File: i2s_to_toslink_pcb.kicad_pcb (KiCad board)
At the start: 2 copper layers, 61.7 x 62.7 mm, 74 parts, among them J1 FTDI_6P, J10 FCR684204T, J11 DIN_DOUT_2TP, J12 MCU_GPIOS, J13 AJ_TP5, J14 C_G0, J15 C_G7, J16 CRST, J17 C_CLKOUT, J2 EXT_CLK_IN5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

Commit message: routing cleanups
Signed-off-by: Mika Laitio <lamikr@gmail.com>
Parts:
- moved C20 3.11 mm to (41.5, 40.3), turned to -90 degrees
- moved R19 2.60 mm to (33.4, 56.0)
- moved R20 2.60 mm to (33.4, 53.4)
- moved J8 1.50 mm to (25.5, 39.0)
- moved C13 1.48 mm to (24.3, 43.3)
- moved U3 1.08 mm to (31.3, 46.7)
- moved C14 1.08 mm to (24.8, 48.9)
- moved C15 1.08 mm to (37.8, 47.6)
- moved C16 1.08 mm to (37.8, 45.0)
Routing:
- net VCC_3V3: track 230.4 -> 222.6 mm
- net Net-(J9-Pin_3): track 28.4 -> 25.7 mm
- net MCU_SDA1: track 56.8 -> 58.7 mm
- net GND: track 95.7 -> 97.6 mm, vias 30 -> 29
- net Net-(J3-Pin_2): track 23.4 -> 25.0 mm
- net EXTERNAL_IN_I2S_BCLK: track 62.1 -> 61.0 mm
- net Net-(J7-Pin_3): track 19.6 -> 18.5 mm
- net MCU_SCL1: track 48.5 -> 49.0 mm

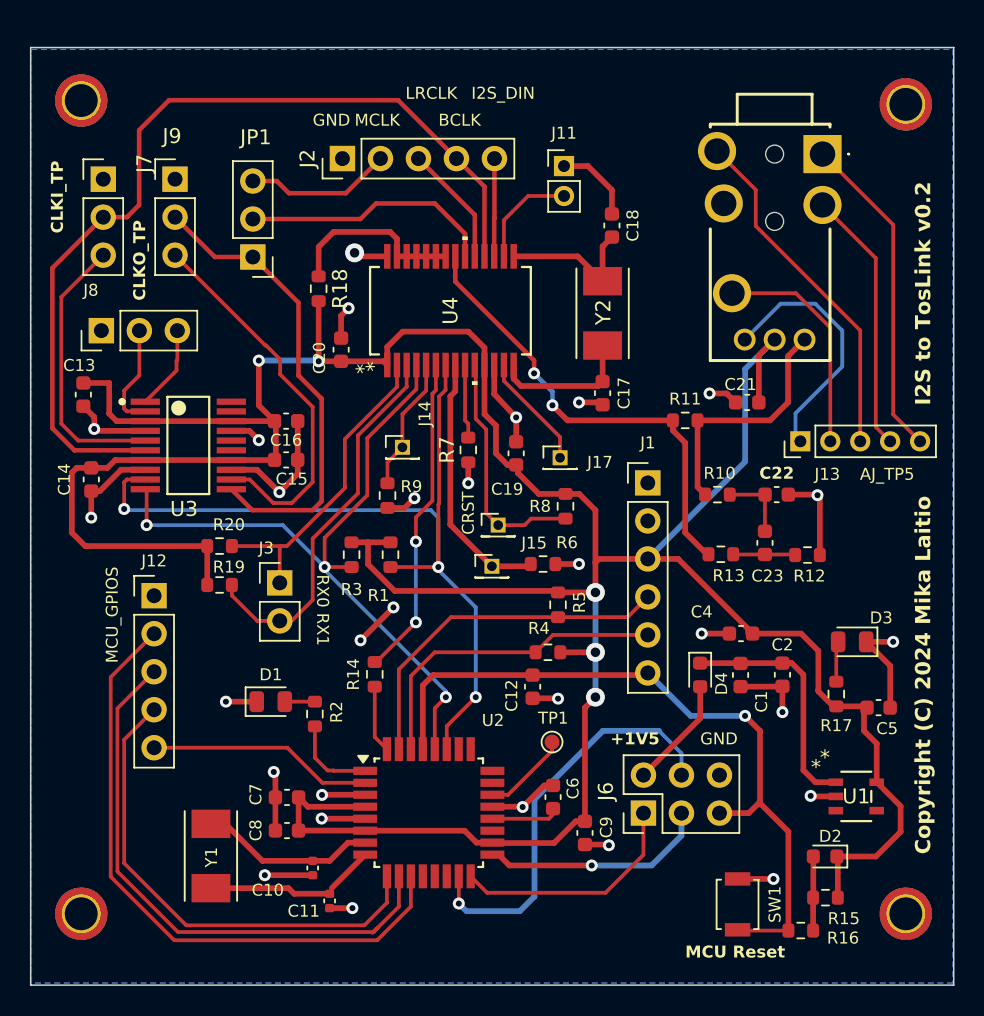
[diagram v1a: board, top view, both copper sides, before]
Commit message: fix toslink pin6 grounding
- had problem already on v1 boards
- move toslink/3.5mm plug little out of board
- re-arrange alternative output

Signed-off-by: Mika Laitio <lamikr@gmail.com>
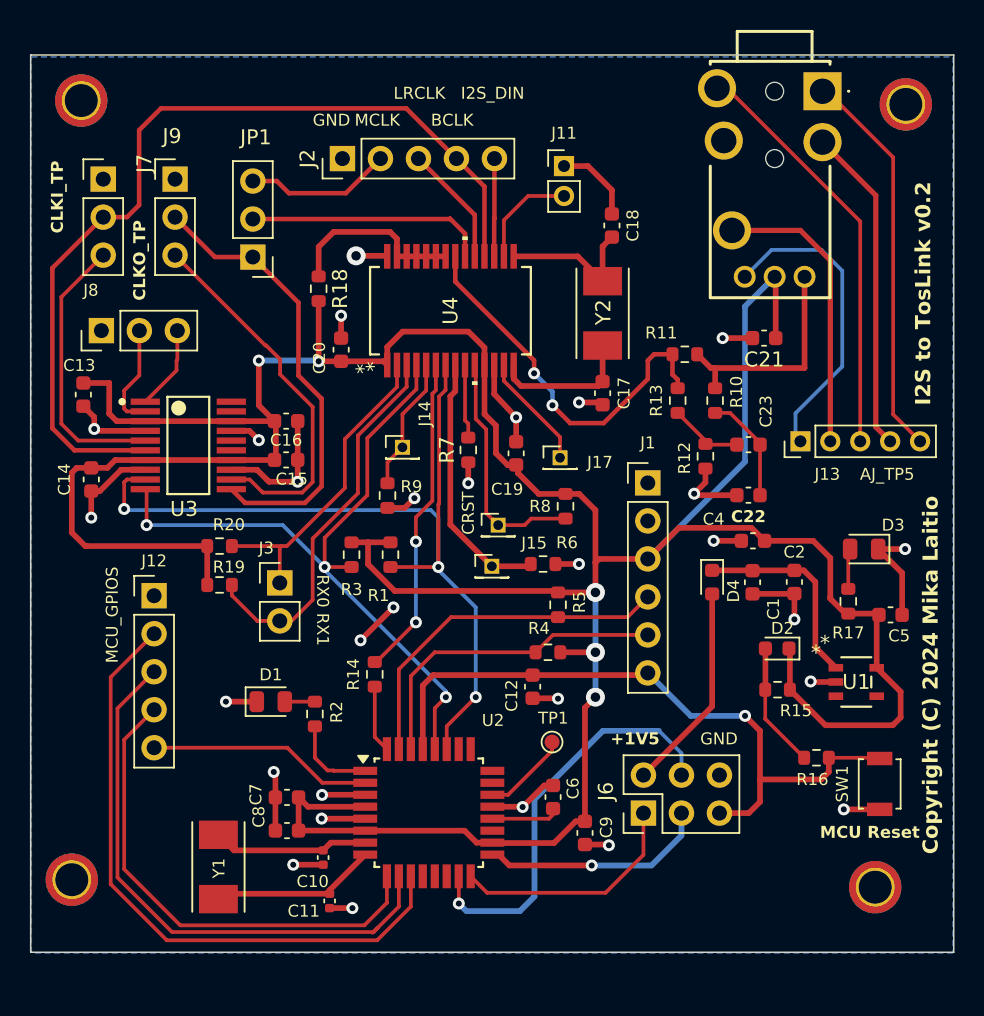
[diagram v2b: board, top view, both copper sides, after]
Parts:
- moved R15 14.3 mm to (70.7, 63.0)
- moved D2 14.3 mm to (70.7, 60.2)
- moved SW1 12.5 mm to (77.5, 69.3), turned to 90 degrees
- moved R16 11.6 mm to (73.3, 67.5), turned to 180 degrees
- moved R13 10.7 mm to (64.0, 43.7), turned to 90 degrees
- moved R12 9.50 mm to (65.9, 47.4), turned to -90 degrees
- moved U1 7.65 mm to (75.9, 62.5)
- moved C23 6.66 mm to (68.7, 46.6), turned to 180 degrees
- moved R10 6.29 mm to (66.5, 43.7), turned to -90 degrees
- moved C1 6.25 mm to (69.0, 55.8)
- moved C2 6.25 mm to (71.8, 55.8)
- moved C4 6.25 mm to (69.0, 53.0)
- moved C5 6.25 mm to (78.2, 58.0)
- moved D4 6.25 mm to (66.3, 55.8)
- moved D3 6.25 mm to (76.5, 53.6)
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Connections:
- J10 pad 6: Net-(J10-GND_2) -> GND
- J13 pad 1: Net-(J10-GND_2) -> GND
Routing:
- net Net-(J10-GND_2): track 17.0 -> 0.00 mm
- net GND: track 97.6 -> 114.5 mm
- net VIN_5V: track 7.48 -> 14.0 mm
- net VCC_3V3: track 222.6 -> 227.9 mm
- net CODEC_OUT_SPDIF_AUDIO_DATA: track 31.0 -> 26.2 mm
- net Net-(J10-LEFT_CHANNEL): track 15.1 -> 19.5 mm
- net Net-(J10-RIGHT_CHANNEL): track 17.7 -> 21.9 mm
- net Net-(J10-DETECTOR_1): track 21.9 -> 26.0 mm
- net Net-(J10-DETECTOR_2): track 23.4 -> 27.3 mm
- net MCU_RST: track 49.1 -> 45.4 mm
- net Net-(D2-A): track 4.89 -> 8.31 mm
- net Net-(D4-K): track 15.8 -> 13.2 mm
- net Net-(C22-Pad1): track 4.80 -> 6.88 mm
- net Net-(J10-VIN): track 16.4 -> 15.0 mm
- net CLKGEN_OUT_I2S_MCLK: track 31.4 -> 30.4 mm
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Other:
- board size 61.7 x 62.7 mm -> 61.7 x 60 mm
